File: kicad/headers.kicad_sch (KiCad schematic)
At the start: 18 parts, among them J1 EX_IO1 (AXU3EGB J15), J2 EX_IO2 (AXU3EGB J16)

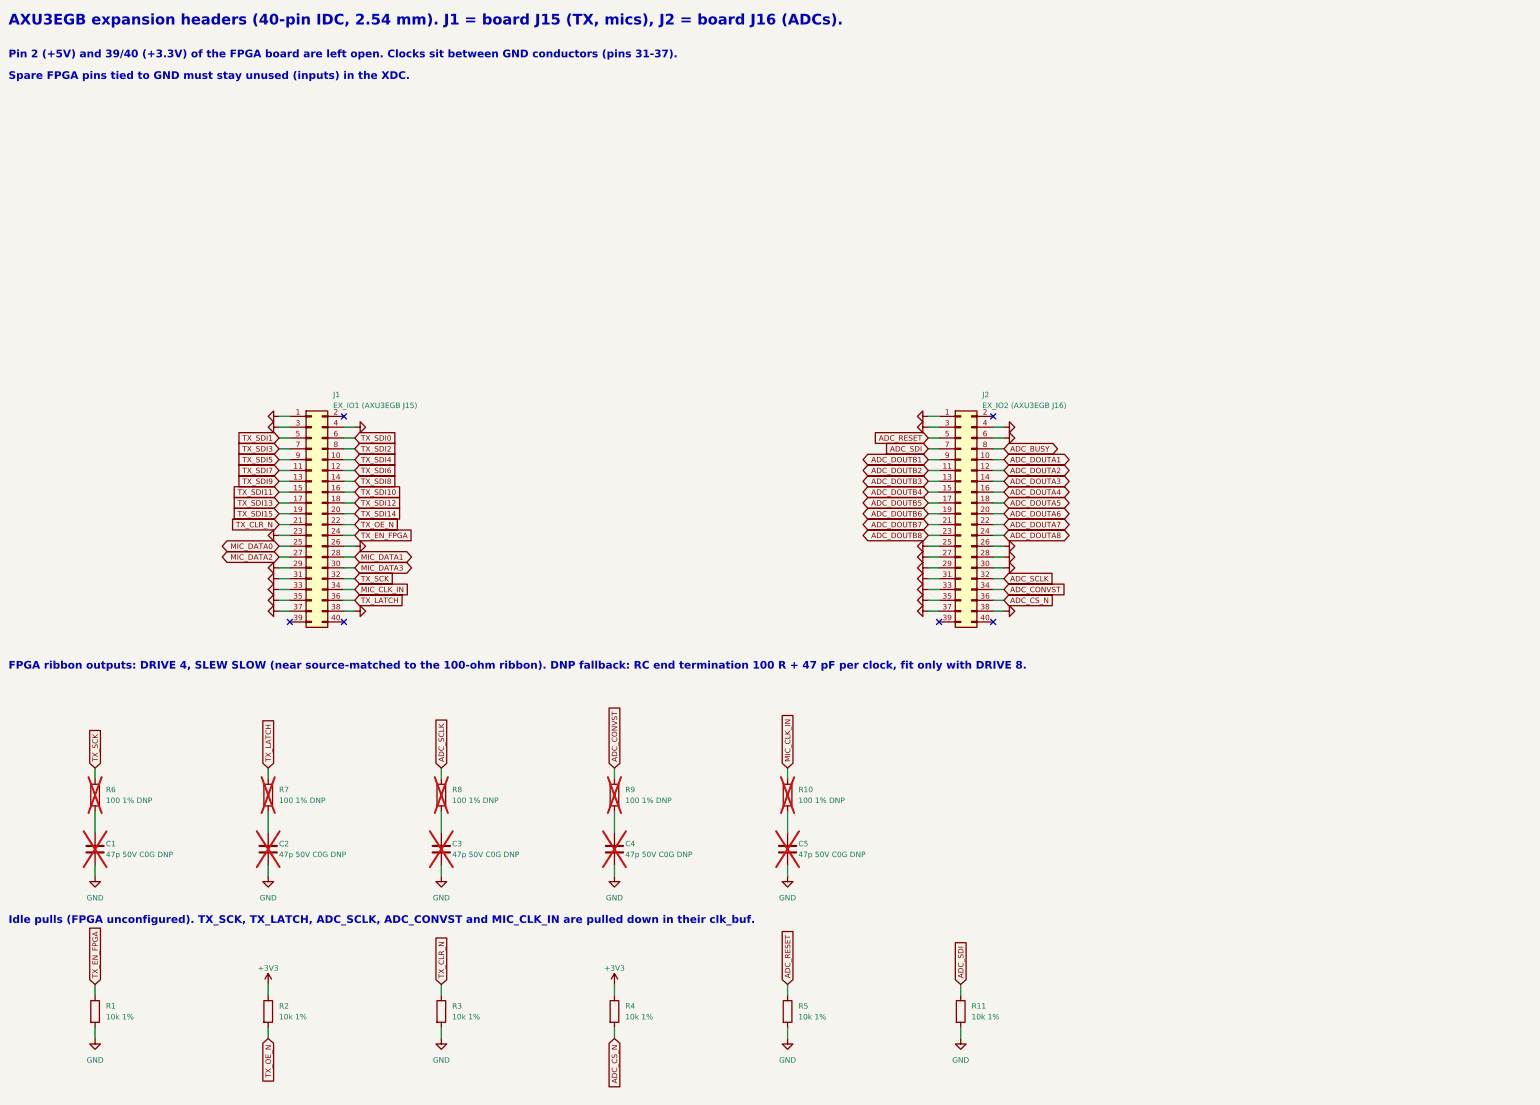
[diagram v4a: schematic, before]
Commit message: Switch to 16 x TLV320ADC5140, +3V3A rail, 3 A buck, datasheet library, transducer DNP
- ADC: 8 x AD7606C-16 ($470/board) -> 16 x TI TLV320ADC5140 at 192 kSPS ($50/board): TDM slave on a
  shared BCLK/FSYNC, I2C (SCL + 4 SDA groups), 2k/1k + 100 nF input network; project symbol from
  scripts/make_symbols.py; 9 clock buffers; J2 remapped
- power: +3V3A (second TPS7A4700, ANY-OUT 3.3 V); +5V buck TPS54202 -> TPS54302 (3 A), L1 10 uH 5 A
- checks and simulations updated for the new ADC input (all 18 checks and 10 sims pass)
- docs/datasheets: a PDF for every part, kept in step by scripts/datasheets.py (run by bom.py)
- design brief section 5a: interface bandwidth budget (no bus is a bottleneck; TX_EDGE = 1)
- CUSA-TR65 marked DNP for JLCPCB (hand-soldered), priced at DigiKey 100+
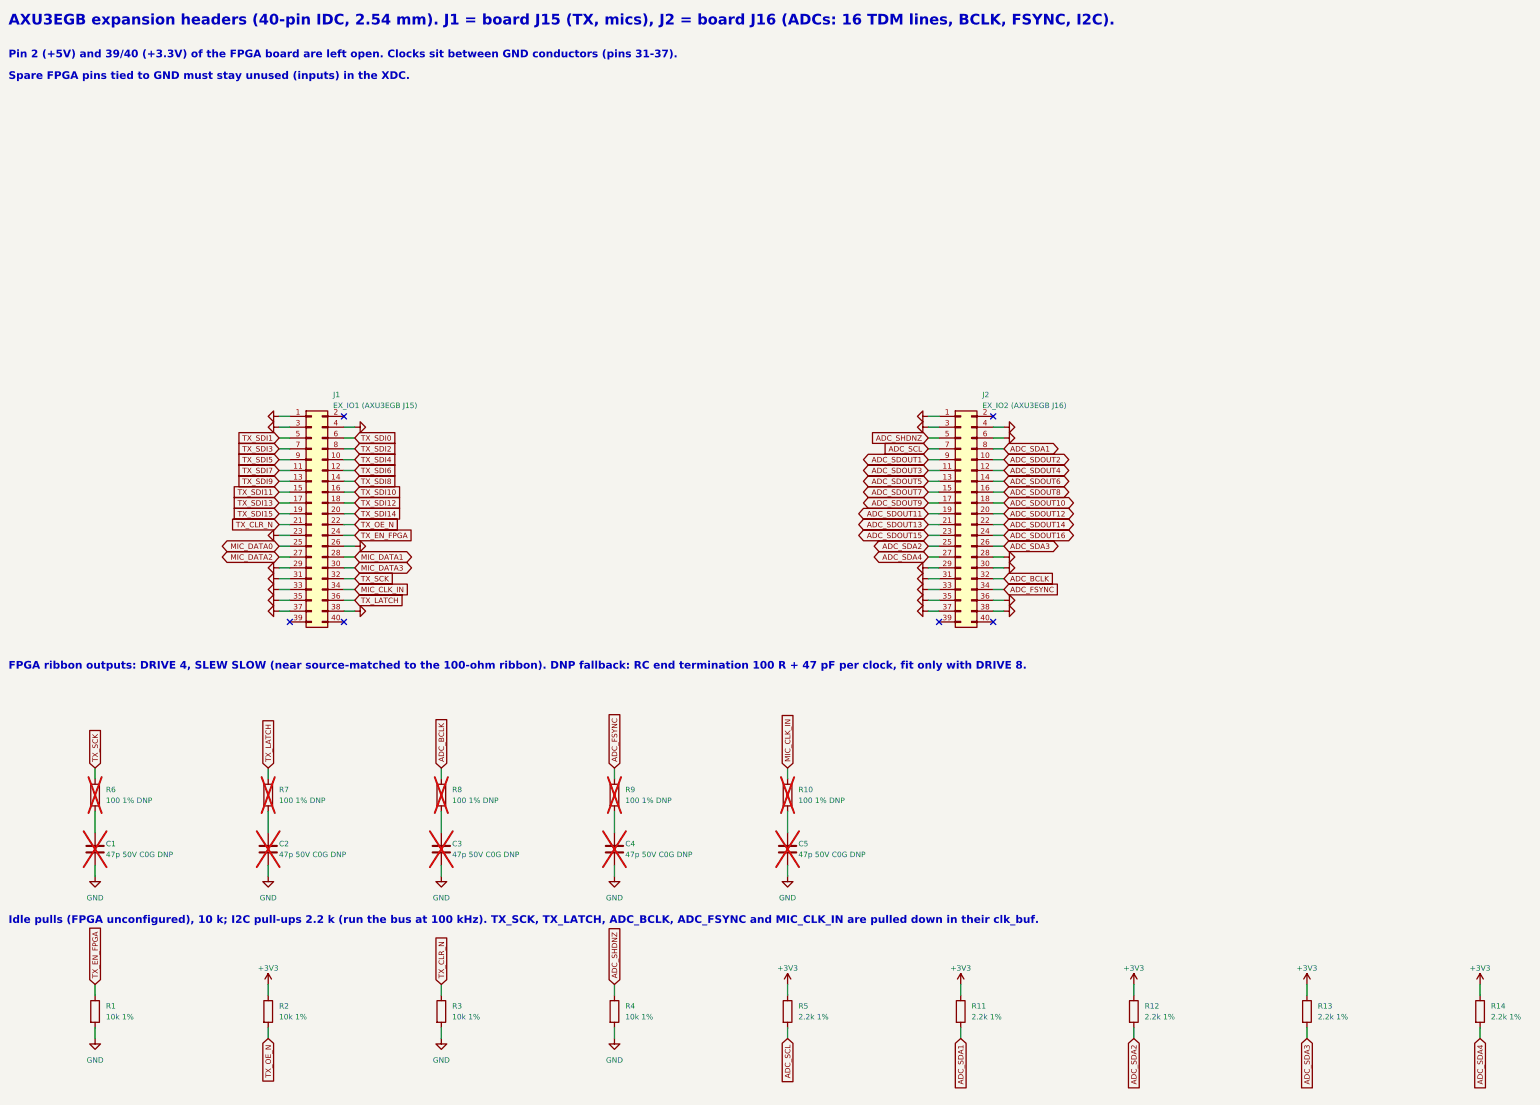
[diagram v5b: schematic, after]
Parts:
- added R12, R13, R14: 2.2k 1%, Resistor_SMD:R_0603_1608Metric, symbol Device:R
- R11, R5: value 10k 1% -> 2.2k 1%; LCSC C25804 -> C4190
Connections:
- net ADC_CS_N is gone; now on net GND: J2.36 (Pin_36), R4.2
- net +3V3: now also R11.1, R5.1, R12.1, R13.1, R14.1; no longer R4.1
- net GND: no longer J2.25 (Pin_25), J2.26 (Pin_26), J2.27 (Pin_27), R11.2, R5.2
- net ADC_BUSY renamed ADC_SDA1
- net ADC_SDA1: now also R11.2
- net ADC_CONVST renamed ADC_FSYNC
- net ADC_DOUTA1 renamed ADC_SDOUT2
- net ADC_DOUTA2 renamed ADC_SDOUT4
- net ADC_DOUTA3 renamed ADC_SDOUT6
- net ADC_DOUTA4 renamed ADC_SDOUT8
- net ADC_DOUTA5 renamed ADC_SDOUT10
- net ADC_DOUTA6 renamed ADC_SDOUT12
- net ADC_DOUTA7 renamed ADC_SDOUT14
- net ADC_DOUTA8 renamed ADC_SDOUT16
- net ADC_DOUTB1 renamed ADC_SDOUT1
- net ADC_DOUTB2 renamed ADC_SDOUT3
- net ADC_DOUTB3 renamed ADC_SDOUT5
- net ADC_DOUTB4 renamed ADC_SDOUT7
- net ADC_DOUTB5 renamed ADC_SDOUT9
- net ADC_DOUTB6 renamed ADC_SDOUT11
- net ADC_DOUTB7 renamed ADC_SDOUT13
- net ADC_DOUTB8 renamed ADC_SDOUT15
- net ADC_RESET renamed ADC_SHDNZ
- net ADC_SHDNZ: now also R4.1; no longer R5.1
- net ADC_SCLK renamed ADC_BCLK
- net ADC_SDI renamed ADC_SCL
- net ADC_SCL: now also R5.2; no longer R11.1
- new net ADC_SDA2: J2.25 (Pin_25), R12.2
- new net ADC_SDA3: J2.26 (Pin_26), R13.2
- new net ADC_SDA4: J2.27 (Pin_27), R14.2
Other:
- note added: "AXU3EGB expansion headers (40-pin IDC, 2.54 mm). J1 = board J15 (TX, mics), J2 = board J16 (ADCs: 16 TDM lines, BCLK, FSYNC, I2C)."
- note added: "Idle pulls (FPGA unconfigured), 10 k; I2C pull-ups 2.2 k (run the bus at 100 kHz). TX_SCK, TX_LATCH, ADC_BCLK, ADC_FSYNC and MIC_CLK_IN are pulled down in their clk_buf."
- note removed: "AXU3EGB expansion headers (40-pin IDC, 2.54 mm). J1 = board J15 (TX, mics), J2 = board J16 (ADCs)."
- note removed: "Idle pulls (FPGA unconfigured). TX_SCK, TX_LATCH, ADC_SCLK, ADC_CONVST and MIC_CLK_IN are pulled down in their clk_buf."

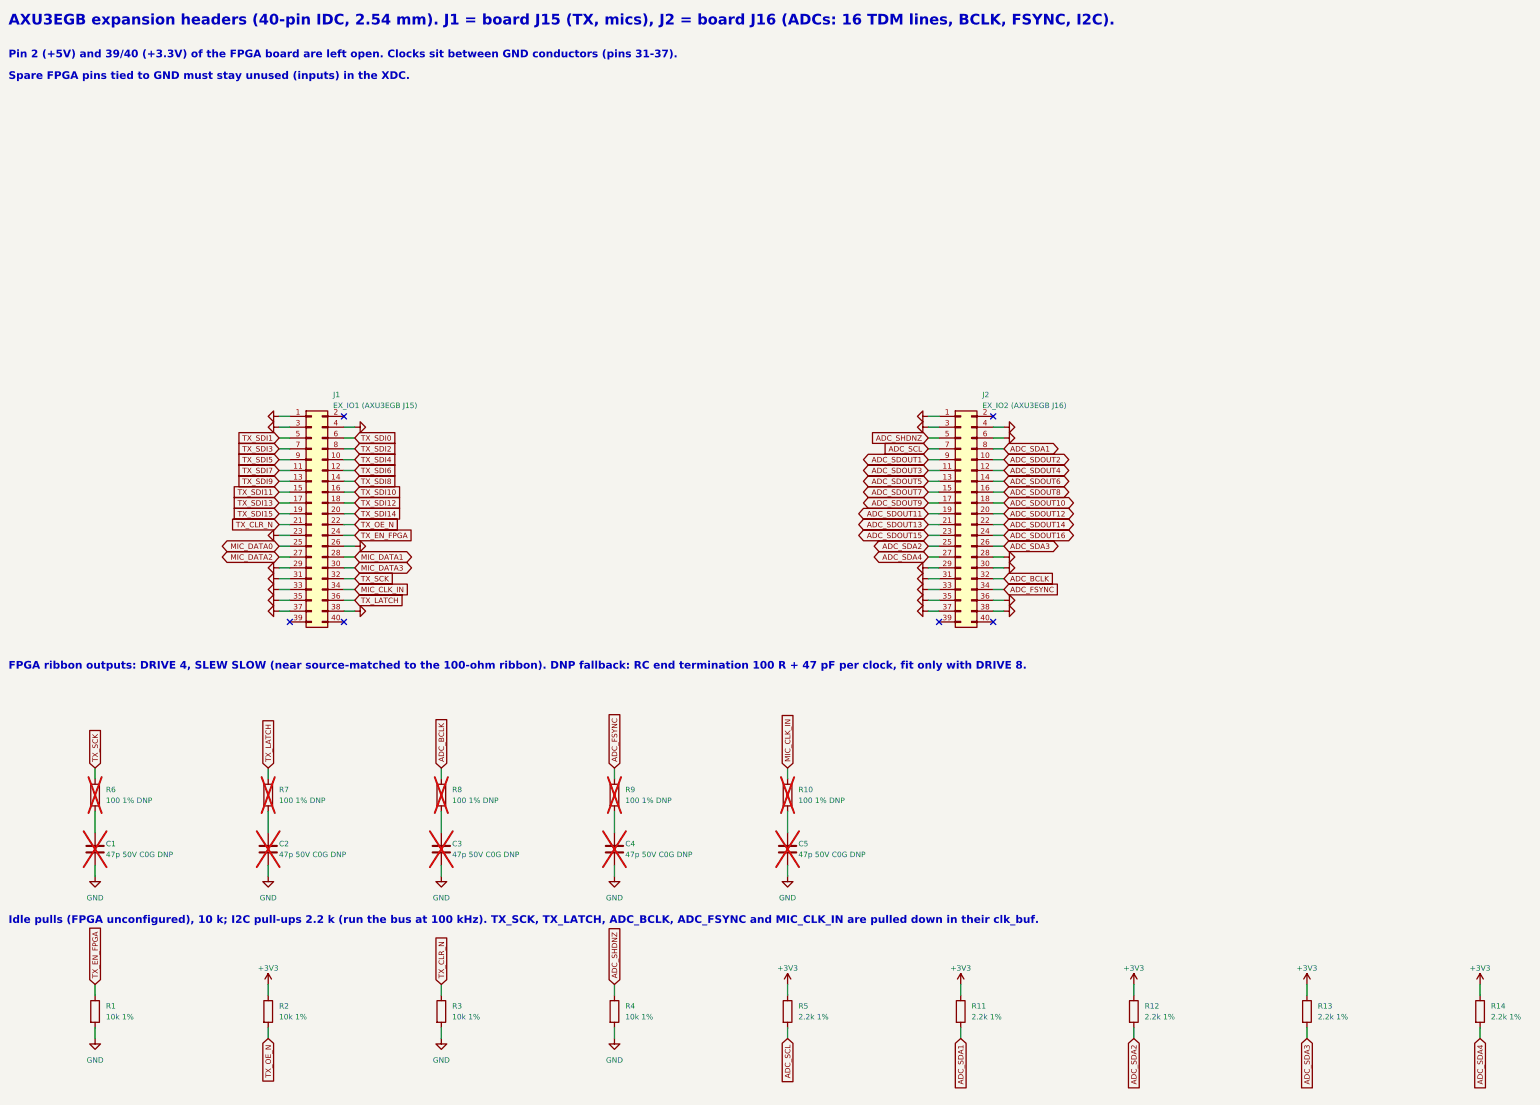
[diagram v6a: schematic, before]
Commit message: Block-first routing: all repeated blocks routed and passing, power input and +-6V5 hand-routed
Schematic
- TX groups and ADC inputs numbered in order (TXG01 = DRV1-4, ADC IN1..4 = RX1..4).
- Power sheets renumbered 1-8 with real references; eFuse RTN no longer tied to GND (TPS2660 9.3.5.5).
- Damped 100 uF bulk caps at the far ends of VIN (C50) and +5V (C51); header clock RC filters removed;
  switch-node snubbers kept as DNP footprints.

Layout and routing
- New routing toolchain: route.py (block stages), block_routes.py (hand-made block routes), maze.py
  (45-degree grid router with rip-up and a per-net time budget), route_lib.py (bend45, chamfer, copper
  checks), block_check.py (DRC and internal nets per block instance), board/cell views.
- Channel, ADC, TX group, clock buffer, enable buffer, mic and header blocks routed and passing
  block_check; no right-angle corners left.
- Designed TX control bus; SDI taps keep 0.7 mm from clock copper.
- Power: 12 V input (eFuse, RTN island, FLT via the front copper) and TPS65131 +-6V5 section with fixed
  templates and hand routing; each power section counts as its own block; the +3V3 LED overflows into
  the gap beside its section.

docs/routing_and_emi.md describes the routing and EMI rules; sim/mic_clock_si adds the mic clock check.
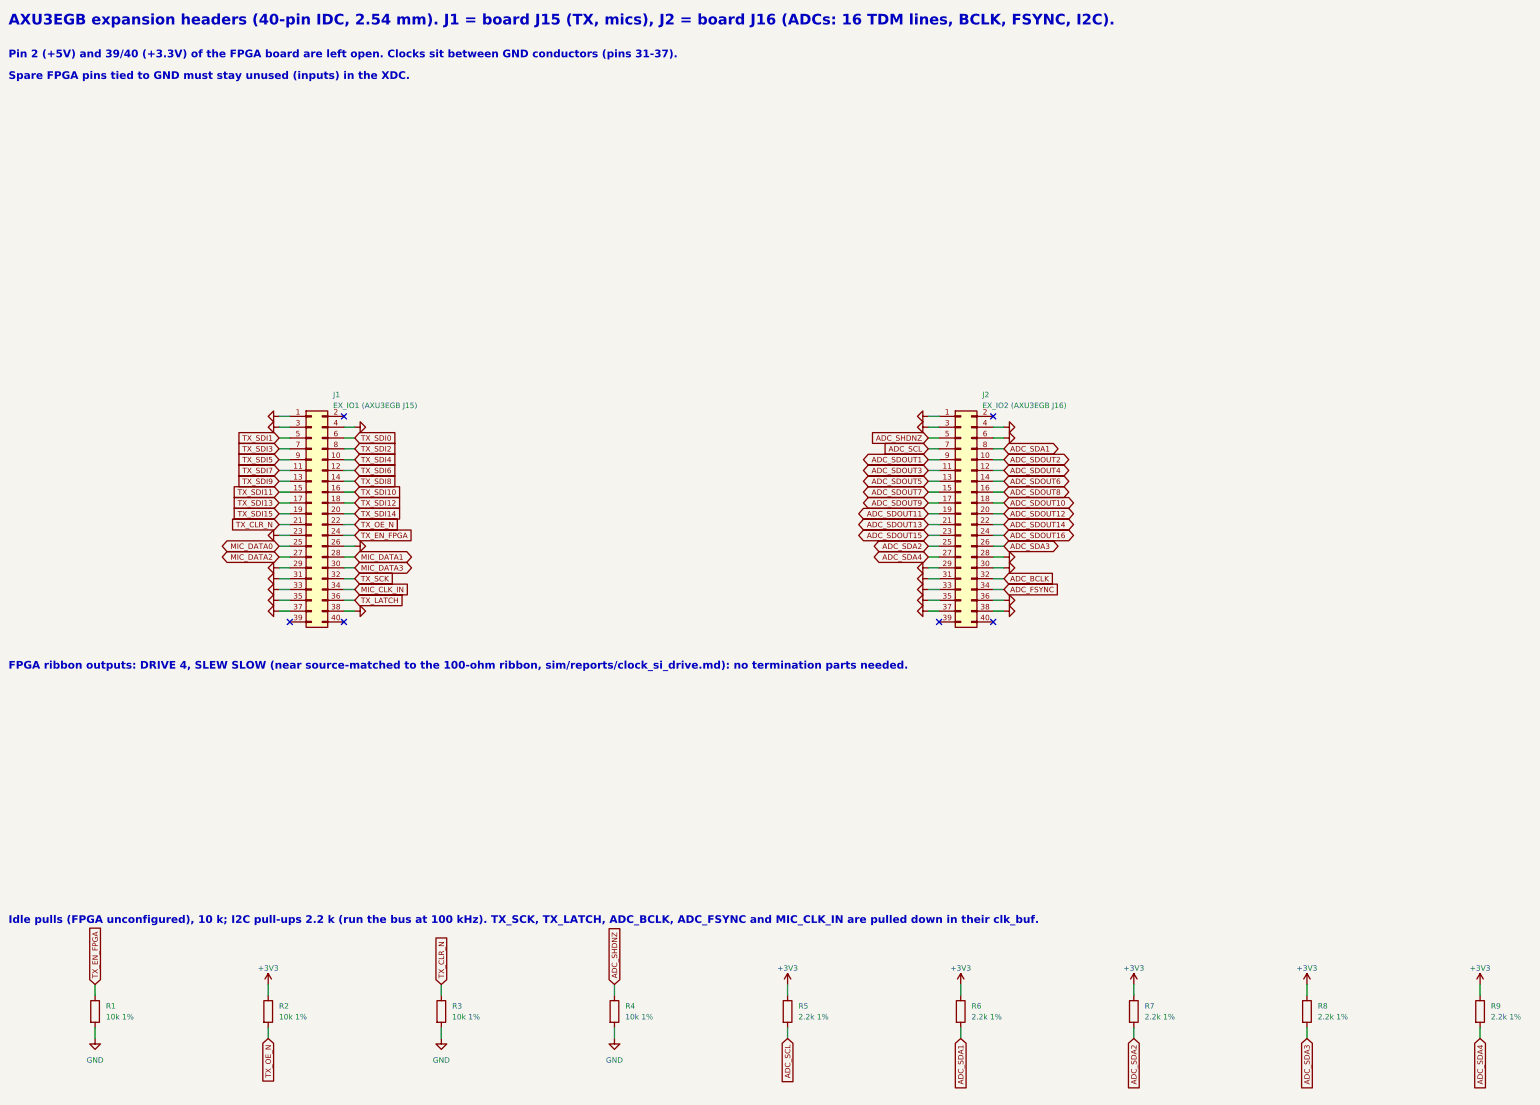
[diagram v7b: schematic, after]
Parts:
- removed C1, C2, C3, C4, C5: 47p 50V C0G DNP, Capacitor_SMD:C_0603_1608Metric, symbol Device:C
- removed R10: 100 1% DNP, Resistor_SMD:R_0603_1608Metric, symbol Device:R
- removed R11, R12, R13, R14: 2.2k 1%, Resistor_SMD:R_0603_1608Metric, symbol Device:R
- R6, R7, R8, R9: value 100 1% DNP -> 2.2k 1%; LCSC C22775 (DNP) -> C4190; now fitted
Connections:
- net +3V3: now also R6.1, R7.1, R8.1, R9.1
- net ADC_BCLK: no longer R8.1
- net ADC_FSYNC: no longer R9.1
- net ADC_SDA1: now also R6.2
- net ADC_SDA2: now also R7.2
- net ADC_SDA3: now also R8.2
- net ADC_SDA4: now also R9.2
- net TX_LATCH: no longer R7.1
- net TX_SCK: no longer R6.1
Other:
- note added: "FPGA ribbon outputs: DRIVE 4, SLEW SLOW (near source-matched to the 100-ohm ribbon, sim/reports/clock_si_drive.md): no termination parts needed."
- note removed: "FPGA ribbon outputs: DRIVE 4, SLEW SLOW (near source-matched to the 100-ohm ribbon). DNP fallback: RC end termination 100 R + 47 pF per clock, fit only with DRIVE 8."
